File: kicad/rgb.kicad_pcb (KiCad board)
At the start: 2 copper layers, 25 parts, among them J1 1935776, J2 Conn_01x05, J3 Conn_01x05, J4 Conn_01x04, J5 Conn_01x02, Q1 DMG9926USD, Q2 DMG9926USD, Q3 DMG9926USD, Q4 DMG9926USD, SW1 SW_Push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

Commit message: pcb layout + mounting
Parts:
- C2: footprint Capacitor_SMD:C_0805_2012Metric_Pad1.15x1.40mm_HandSolder -> Capacitor_SMD:C_0603_1608Metric_Pad1.08x0.95mm_HandSolder; moved to B.Cu
- C3: moved to B.Cu
- moved C2 128.0 mm to (160.5, 65.8), turned to 180 degrees
- moved R3 119.4 mm to (151.5, 94.6), turned to 270 degrees
- moved R1 114.0 mm to (165.9, 62.9), turned to 90 degrees
- moved D1 109.2 mm to (148.7, 94.7), turned to 270 degrees
- moved R2 102.0 mm to (151.6, 62.1), turned to 180 degrees
- moved U2 100.2 mm to (160.4, 63.3)
- moved C1 100.1 mm to (180.5, 84.2)
- moved J1 100.1 mm to (188.8, 83.8)
- moved J2 100.1 mm to (177.5, 91.2)
- moved J3 100.1 mm to (188.5, 65.0)
- moved J4 100.1 mm to (128.1, 94.3)
- moved J5 100.1 mm to (136.9, 94.3)
- moved Q1 100.1 mm to (169.9, 86.2)
- moved Q2 100.1 mm to (160.0, 86.1)
- moved Q3 100.1 mm to (181.0, 70.0)
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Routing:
- net +5V: track 37.1 -> 110.8 mm, vias 1 -> 2
- net /PWR_EN: track 2.72 -> 23.0 mm, vias 0 -> 2
- net Net-(R1-Pad1): track 0.62 -> 11.5 mm
- net Net-(D1-Pad1): track 0.00 -> 2.84 mm
- net GND: track 0.00 -> 1.29 mm, vias 0 -> 1
- net (no net): vias 0 -> 4
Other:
- board outline added: 74 x 44 mm

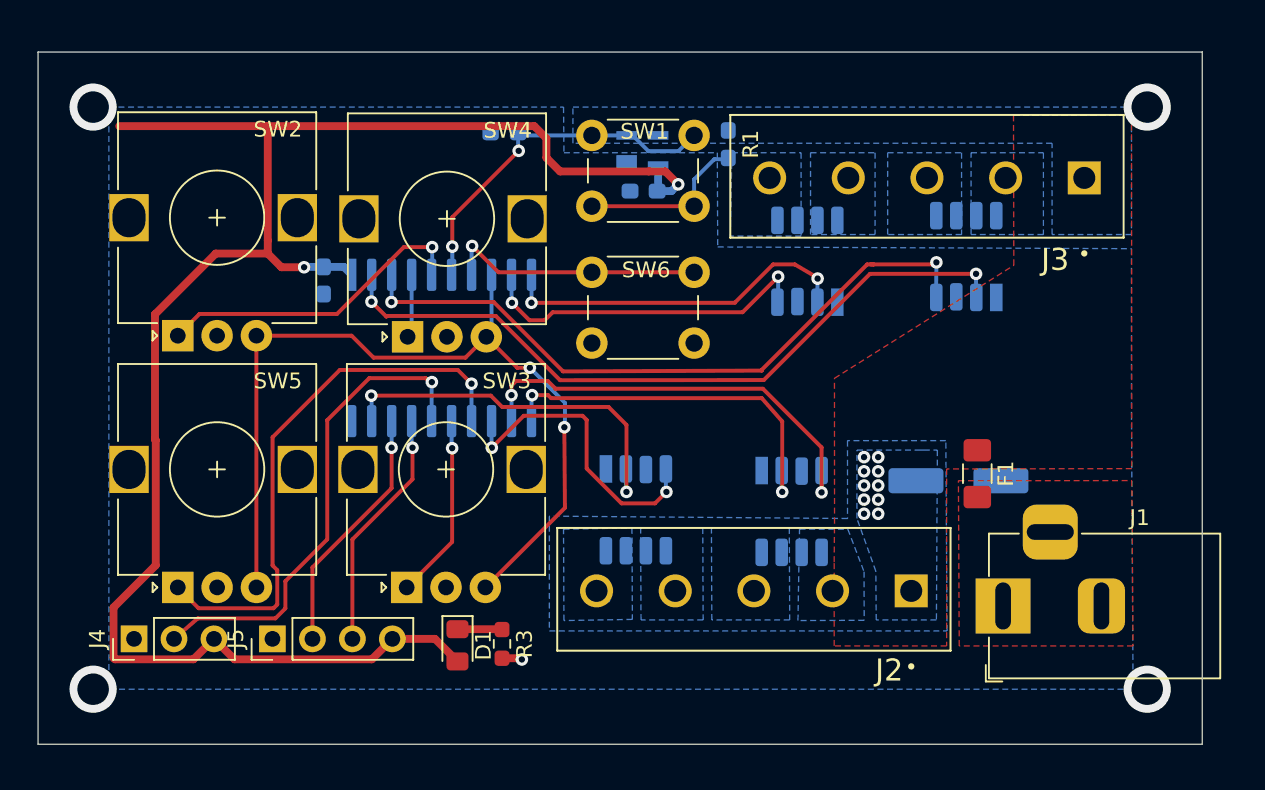
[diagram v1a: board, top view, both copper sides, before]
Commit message: New PCB formfactor
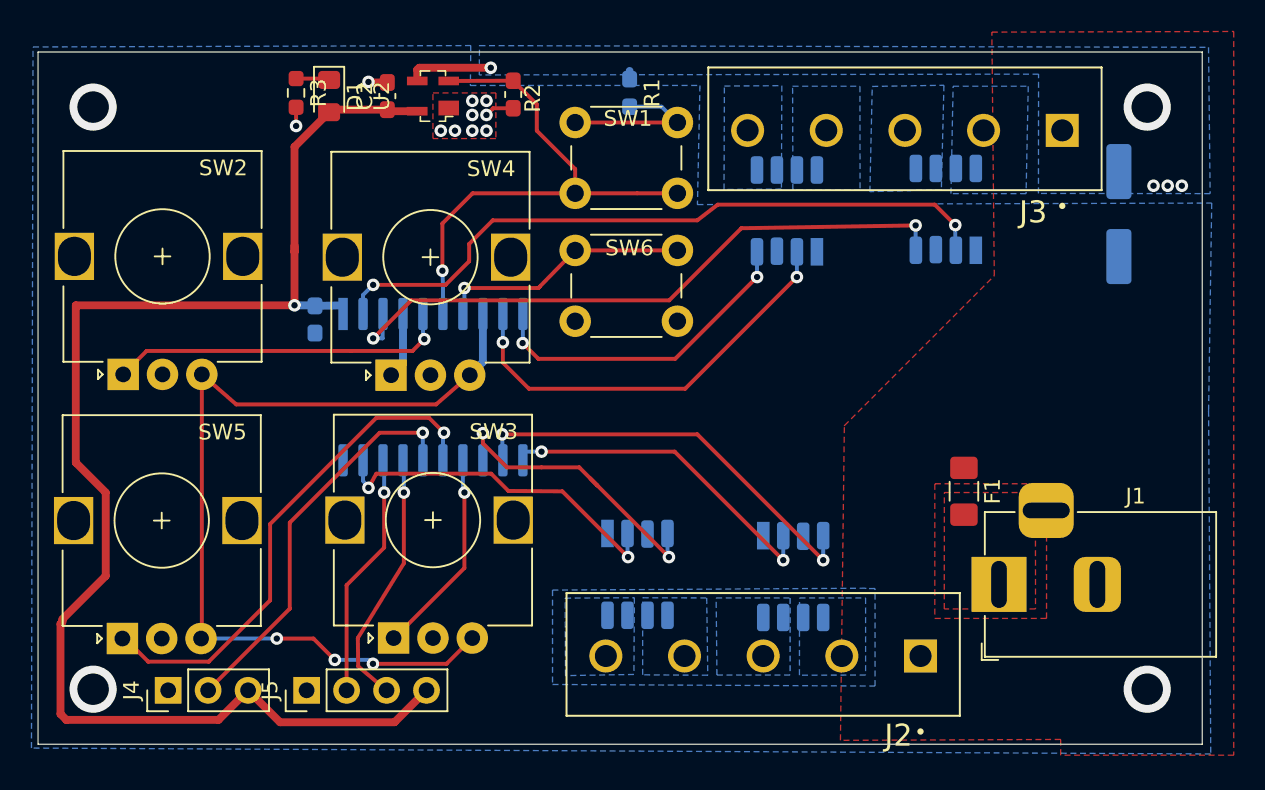
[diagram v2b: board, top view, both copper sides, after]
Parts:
- C2, R2, U2: moved to F.Cu
- moved R3 37.4 mm to (138.4, 59.6)
- moved D1 35.9 mm to (140.5, 59.8)
- moved C1 19.8 mm to (190.7, 67.3), turned to 270 degrees
- moved C2 17.4 mm to (144.2, 59.8), turned to 90 degrees
- moved U2 13.8 mm to (147.1, 59.8)
- moved R1 7.07 mm to (159.6, 59.6)
- moved SW5 4.79 mm to (129.9, 86.0)
- moved SW2 4.25 mm to (129.9, 69.2)
- moved J2 4.18 mm to (178.1, 95.4)
- moved Q1 4.14 mm to (170.0, 90.3)
- moved Q2 4.10 mm to (160.1, 90.2)
- moved J4 3.92 mm to (130.3, 97.6)
- moved J5 3.92 mm to (139.1, 97.6)
- moved Q4 3.45 mm to (169.6, 67.1)
- moved J3 3.33 mm to (187.1, 62.0)
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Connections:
- SW1 pad 1: Net-(R1-Pad1) -> /PWR_EN
- SW1 pad 2: /PWR_EN -> Net-(R1-Pad1)
- U1 pad 10: /PWM_7 -> /PWM_8
- U1 pad 14: /SW5_A -> /SW3_A
- U1 pad 15: /SW3_A -> /SW5_A
- U1 pad 9: /PWM_8 -> /PWM_7
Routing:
- net +5V: track 110.8 -> 90.3 mm, vias 2 -> 1
- net /PWR_EN: track 23.0 -> 35.0 mm, vias 2 -> 1
- net +12V: track 0.00 -> 6.13 mm, vias 10 -> 4
- net /RESET: track 31.2 -> 25.4 mm
- net /PWM_7: track 22.7 -> 27.0 mm
- net GND: track 1.29 -> 4.96 mm, vias 1 -> 10
- net /PWM_2: track 24.2 -> 20.7 mm
- net /PWM_5: track 46.8 -> 44.0 mm
- net /SW5_A: track 34.9 -> 32.7 mm
- net /SW_B: track 56.4 -> 58.5 mm, vias 2 -> 3
- net /SW2_A: track 20.3 -> 22.3 mm
- net /PWM_4: track 24.4 -> 22.7 mm
- net /PWM_6: track 43.7 -> 42.1 mm
- net /SW3_A: track 11.8 -> 13.4 mm
- net Net-(R1-Pad1): track 11.5 -> 9.96 mm
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- added copper zone on F.Cu, net GND

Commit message: minor layout changes
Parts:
- R1: moved to F.Cu
- moved R1 6.04 mm to (153.6, 60.3)
- moved R2 0.72 mm to (151.8, 60.3)
- moved D1 0.67 mm to (140.2, 60.4)
- moved R3 0.67 mm to (138.1, 60.2)
- moved U2 0.60 mm to (147.1, 60.4)
- moved C2 0.51 mm to (144.3, 60.3)
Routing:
- net Net-(R1-Pad1): track 9.96 -> 13.3 mm
- net +12V: track 6.13 -> 9.40 mm
- net /PWR_EN: track 35.0 -> 34.2 mm
- net GND: track 4.96 -> 4.29 mm
- net +5V: track 90.3 -> 89.7 mm

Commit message: dcdc layout
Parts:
- added TP1: TestPoint, TestPoint:TestPoint_Pad_D2.0mm, F.Cu at (171.5, 85.0)
- added TP2: TestPoint, TestPoint:TestPoint_Pad_D2.0mm, F.Cu at (237.0, 77.6)
- added TP3: TestPoint, TestPoint:TestPoint_Pad_D2.0mm, F.Cu at (210.3, 72.7)
- added TP4: TestPoint, TestPoint:TestPoint_Pad_D2.0mm, F.Cu at (210.3, 76.8)
- added TP5: TestPoint, TestPoint:TestPoint_Pad_D2.0mm, F.Cu at (214.4, 72.7)
- added TP6: TestPoint, TestPoint:TestPoint_Pad_D2.0mm, F.Cu at (214.4, 76.8)
- added TP7: TestPoint, TestPoint:TestPoint_Pad_D2.0mm, F.Cu at (218.4, 72.7)
- added TP8: TestPoint, TestPoint:TestPoint_Pad_D2.0mm, F.Cu at (218.4, 76.8)
- moved D1 2.47 mm to (137.8, 61.0), turned to 0 degrees
- moved R1 1.92 mm to (151.9, 59.4), turned to 180 degrees
- moved R2 1.02 mm to (152.0, 61.3), turned to 180 degrees
- moved R3 1.00 mm to (138.0, 59.2), turned to 0 degrees
- moved C1 0.10 mm to (190.7, 67.2)
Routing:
- net /PWM_1: track 26.9 -> 29.7 mm
- net +5V: track 89.7 -> 92.2 mm
- net Net-(R1-Pad1): track 13.3 -> 15.3 mm
- net +12V: track 9.40 -> 7.74 mm
- net /PWR_EN: track 34.2 -> 35.2 mm
- net GND: track 4.29 -> 4.83 mm, vias 10 -> 12
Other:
- board text added: "Designed by: - Jeremie Lavoie - Alexandre Gauthier"
- board text added: "RGBW Driver"
- board text added: "Schematics and firmware:"
- board text added: "github.com/AlexandreGauthier/rgb"

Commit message: this dummy wants his name spelled right
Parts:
- moved TP2 72.5 mm to (165.4, 88.7)
- moved TP4 54.9 mm to (156.8, 88.7)
- moved TP3 50.1 mm to (162.0, 85.7)
- moved TP7 48.3 mm to (170.2, 74.7)
- moved TP8 45.7 mm to (173.1, 71.2)
- moved TP6 37.6 mm to (177.2, 71.4)
- moved TP5 34.0 mm to (180.4, 71.4)
- moved TP1 5.75 mm to (167.1, 81.3)
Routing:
- net /PWM_8: track 20.9 -> 27.5 mm
- net /PWM_6: track 42.0 -> 46.3 mm
- net /PWM_5: track 43.9 -> 47.3 mm
- net /PWM_2: track 20.7 -> 23.1 mm
- net /PWM_3: track 19.4 -> 21.8 mm
- net /PWM_4: track 22.7 -> 24.9 mm
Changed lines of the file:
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@@
     (thickness 1.6)
     (drawings 12)
-    (tracks 266)
+    (tracks 289)
     (zones 0)
     (modules 33)
@@
   (page A4)
   (layers
-    (0 F.Cu signal)
-    (31 B.Cu signal)
+    (0 F.Cu signal hide)
+    (31 B.Cu signal hide)
     (32 B.Adhes user)
     (33 F.Adhes user)
@@
   )
   (module TestPoint:TestPoint_Pad_D2.0mm (layer F.Cu)
-    (at 218.45 76.75)
+    (at 173.1 71.2)
     (descr "SMD pad as test Point, diameter 2.0mm")
     (tags "test point SMD pad")
@@
   )
   (module TestPoint:TestPoint_Pad_D2.0mm (layer F.Cu)
-    (at 218.45 72.7)
+    (at 170.2 74.7)
     (descr "SMD pad as test Point, diameter 2.0mm")
     (tags "test point SMD pad")
@@
   )
   (module TestPoint:TestPoint_Pad_D2.0mm (layer F.Cu)
-    (at 214.4 76.75)
+    (at 177.2 71.4)
     (descr "SMD pad as test Point, diameter 2.0mm")
     (tags "test point SMD pad")
@@
   )
   (module TestPoint:TestPoint_Pad_D2.0mm (layer F.Cu)
-    (at 214.4 72.7)
+    (at 180.4 71.4)
     (descr "SMD pad as test Point, diameter 2.0mm")
     (tags "test point SMD pad")
@@
   )
   (module TestPoint:TestPoint_Pad_D2.0mm (layer F.Cu)
-    (at 210.35 76.75)
+    (at 156.8 88.7)
     (descr "SMD pad as test Point, diameter 2.0mm")
     (tags "test point SMD pad")
@@
   )
   (module TestPoint:TestPoint_Pad_D2.0mm (layer F.Cu)
-    (at 210.35 72.7)
+    (at 162 85.7)
     (descr "SMD pad as test Point, diameter 2.0mm")
     (tags "test point SMD pad")
@@
   )
   (module TestPoint:TestPoint_Pad_D2.0mm (layer F.Cu)
-    (at 237 77.6)
+    (at 165.4 88.7)
     (descr "SMD pad as test Point, diameter 2.0mm")
     (tags "test point SMD pad")
@@
   )
   (module TestPoint:TestPoint_Pad_D2.0mm (layer F.Cu)
-    (at 171.5 85)
+    (at 167.1 81.3)
     (descr "SMD pad as test Point, diameter 2.0mm")
     (tags "test point SMD pad")
@@
     )
   )
-  (gr_text github.com/AlexandreGauthier/rgb (at 194.9 70.3 90) (layer F.SilkS)
+  (gr_text github.com/AlexandreGauthier/rgb (at 162.5 100) (layer F.SilkS)
     (effects (font (size 1 1) (thickness 0.15) italic))
   )
-  (gr_text "Schematics and firmware:" (at 193.4 73.7 90) (layer F.SilkS)
+  (gr_text "Schematics and firmware:" (at 138.8 100.1) (layer F.SilkS)
     (effects (font (size 1 1) (thickness 0.15)))
   )
-  (gr_text "Designed by:\n - Jeremie Lavoie\n - Alexandre Gauthier\n" (at 177.4 84.5 90) (layer F.SilkS)
+  (gr_text "Designed by:\n - Jeremie Lavoie\n - Alexandre Gauthier\n" (at 172.7 78.6) (layer F.SilkS)
     (effects (font (size 1 1) (thickness 0.15)) (justify left))
   )
-  (gr_text "RGBW Driver" (at 172.4 75.5 90) (layer F.SilkS)
+  (gr_text "RGBW Driver" (at 181.9 74.7) (layer F.SilkS)
     (effects (font (size 2 2) (thickness 0.3)))
   )
@@
   (segment (start 153.365 82.4) (end 153.1 82.4) (width 0.25) (layer B.Cu) (net 2))
   (segment (start 154 82.4) (end 162.465 82.4) (width 0.25) (layer F.Cu) (net 2))
-  (segment (start 162.465 82.4) (end 169.365 89.3) (width 0.25) (layer F.Cu) (net 2))
+  (segment (start 167.0325 87.0675) (end 167.0325 86.9675) (width 0.25) (layer F.Cu) (net 2))
+  (segment (start 165.4 88.7) (end 167.0325 87.0675) (width 0.25) (layer F.Cu) (net 2))
+  (segment (start 167.0325 86.9675) (end 169.365 89.3) (width 0.25) (layer F.Cu) (net 2))
+  (segment (start 162.465 82.4) (end 167.0325 86.9675) (width 0.25) (layer F.Cu) (net 2))
   (segment (start 171.905 89.095) (end 171.905 89.095) (width 0.25) (layer B.Cu) (net 3))
   (segment (start 171.905 87.74) (end 171.905 89.3) (width 0.25) (layer B.Cu) (net 3))
@@
   (via (at 151.5 81.3) (size 0.8) (drill 0.4) (layers F.Cu B.Cu) (net 3))
   (segment (start 151.5 81.3) (end 163.905 81.3) (width 0.25) (layer F.Cu) (net 3))
-  (segment (start 169.6025 86.8975) (end 171.5 85) (width 0.25) (layer F.Cu) (net 3))
-  (segment (start 163.905 81.3) (end 169.5025 86.8975) (width 0.25) (layer F.Cu) (net 3))
   (segment (start 169.5025 86.8975) (end 169.6025 86.8975) (width 0.25) (layer F.Cu) (net 3))
   (segment (start 169.5025 86.8975) (end 171.905 89.3) (width 0.25) (layer F.Cu) (net 3))
+  (segment (start 165.7025 82.6975) (end 167.1 81.3) (width 0.25) (layer F.Cu) (net 3))
+  (segment (start 165.7025 83.0975) (end 169.5025 86.8975) (width 0.25) (layer F.Cu) (net 3))
+  (segment (start 165.7025 82.6975) (end 165.5025 82.8975) (width 0.25) (layer F.Cu) (net 3))
+  (segment (start 165.5025 82.8975) (end 165.7025 83.0975) (width 0.25) (layer F.Cu) (net 3))
+  (segment (start 163.905 81.3) (end 165.5025 82.8975) (width 0.25) (layer F.Cu) (net 3))
   (segment (start 159.5 89.1) (end 159.5 89.1) (width 0.25) (layer F.Cu) (net 4))
   (segment (start 142.655 84.255) (end 142.655 82.95) (width 0.25) (layer B.Cu) (net 4))
@@
   (segment (start 151.9 84.9) (end 150.8 83.8) (width 0.25) (layer F.Cu) (net 4))
   (segment (start 155.324999 84.924999) (end 151.9 84.9) (width 0.25) (layer F.Cu) (net 4))
-  (segment (start 159.5 89.1) (end 155.324999 84.924999) (width 0.25) (layer F.Cu) (net 4))
   (segment (start 150.8 83.8) (end 143.5 83.8) (width 0.25) (layer F.Cu) (net 4))
   (segment (start 159.465 89.065) (end 159.465 87.6) (width 0.25) (layer B.Cu) (net 4))
   (segment (start 159.5 89.1) (end 159.465 89.065) (width 0.25) (layer B.Cu) (net 4))
   (via (at 159.5 89.1) (size 0.8) (drill 0.4) (layers F.Cu B.Cu) (net 4))
+  (segment (start 157.7 87.8) (end 156.4 89.1) (width 0.25) (layer F.Cu) (net 4))
+  (segment (start 157.7 87.3) (end 155.324999 84.924999) (width 0.25) (layer F.Cu) (net 4))
+  (segment (start 157.7 87.8) (end 157.95 87.55) (width 0.25) (layer F.Cu) (net 4))
+  (segment (start 157.95 87.55) (end 157.7 87.3) (width 0.25) (layer F.Cu) (net 4))
+  (segment (start 159.5 89.1) (end 157.95 87.55) (width 0.25) (layer F.Cu) (net 4))
   (segment (start 162.1 89.1) (end 162.1 89.1) (width 0.25) (layer F.Cu) (net 5))
   (segment (start 150.275 82.95) (end 150.275 81.225) (width 0.25) (layer B.Cu) (net 5))
@@
   (segment (start 154 83.4) (end 156.4 83.4) (width 0.25) (layer F.Cu) (net 5))
   (segment (start 157.1 84.1) (end 157.55 84.55) (width 0.25) (layer F.Cu) (net 5))
-  (segment (start 157.55 84.55) (end 162 89.1) (width 0.25) (layer F.Cu) (net 5))
   (segment (start 162.005 89.195) (end 162.005 87.6) (width 0.25) (layer B.Cu) (net 5))
   (segment (start 162 89.1) (end 162.005 89.195) (width 0.25) (layer B.Cu) (net 5))
   (via (at 162 89.1) (size 0.8) (drill 0.4) (layers F.Cu B.Cu) (net 5))
+  (segment (start 160.521111 87.178889) (end 162 85.7) (width 0.25) (layer F.Cu) (net 5))
+  (segment (start 157.55 84.55) (end 160.121111 87.178889) (width 0.25) (layer F.Cu) (net 5))
+  (segment (start 160.521111 87.178889) (end 160.318889 87.381111) (width 0.25) (layer F.Cu) (net 5))
+  (segment (start 160.318889 87.381111) (end 162 89.1) (width 0.25) (layer F.Cu) (net 5))
+  (segment (start 160.121111 87.178889) (end 160.318889 87.381111) (width 0.25) (layer F.Cu) (net 5))
   (via (at 152.8 75.5) (size 0.8) (drill 0.4) (layers F.Cu B.Cu) (net 6))
   (segment (start 152.815 75.485) (end 152.8 75.5) (width 0.25) (layer B.Cu) (net 6))
@@
   (segment (start 162.5 76.5) (end 153.8 76.5) (width 0.25) (layer F.Cu) (net 6))
   (via (at 167.7 71.2) (size 0.8) (drill 0.4) (layers F.Cu B.Cu) (net 6))
+  (segment (start 167.7 71.2) (end 169.2 69.7) (width 0.25) (layer F.Cu) (net 6))
+  (segment (start 171.6 69.7) (end 173.1 71.2) (width 0.25) (layer F.Cu) (net 6))
+  (segment (start 169.2 69.7) (end 171.6 69.7) (width 0.25) (layer F.Cu) (net 6))
   (segment (start 151.545 73.65) (end 151.545 75.455) (width 0.25) (layer B.Cu) (net 7))
   (segment (start 151.545 75.455) (end 151.545 75.455) (width 0.25) (layer B.Cu) (net 7))
@@
   (segment (start 162.115001 72.784999) (end 145.715001 72.784999) (width 0.25) (layer F.Cu) (net 8))
   (via (at 177.778688 68.1) (size 0.8) (drill 0.4) (layers F.Cu B.Cu) (net 8))
+  (segment (start 177.778688 70.821312) (end 177.2 71.4) (width 0.25) (layer F.Cu) (net 8))
+  (segment (start 177.2 71.4) (end 177.2 70.2) (width 0.25) (layer F.Cu) (net 8))
+  (segment (start 177.778688 69.621312) (end 177.778688 68.1) (width 0.25) (layer F.Cu) (net 8))
+  (segment (start 177.2 70.2) (end 177.778688 69.621312) (width 0.25) (layer F.Cu) (net 8))
   (segment (start 142.655 72.445) (end 142.655 73.65) (width 0.25) (layer B.Cu) (net 9))
   (segment (start 143.3 71.8) (end 142.655 72.445) (width 0.25) (layer B.Cu) (net 9))
@@
   (segment (start 180.3 68.1) (end 179 66.7) (width 0.25) (layer F.Cu) (net 9))
   (via (at 180.3 68.1) (size 0.8) (drill 0.4) (layers F.Cu B.Cu) (net 9))
+  (segment (start 180.3 71.3) (end 180.4 71.4) (width 0.25) (layer F.Cu) (net 9))
+  (segment (start 180.3 68.1) (end 180.3 71.3) (width 0.25) (layer F.Cu) (net 9))
   (via (at 192.4 65.5) (size 0.8) (drill 0.4) (layers F.Cu B.Cu) (net 10))
   (via (at 192.4 64.6) (size 0.8) (drill 0.4) (layers F.Cu B.Cu) (net 10))
